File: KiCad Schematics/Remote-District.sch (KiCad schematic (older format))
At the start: 13 parts, among them M1 Fan

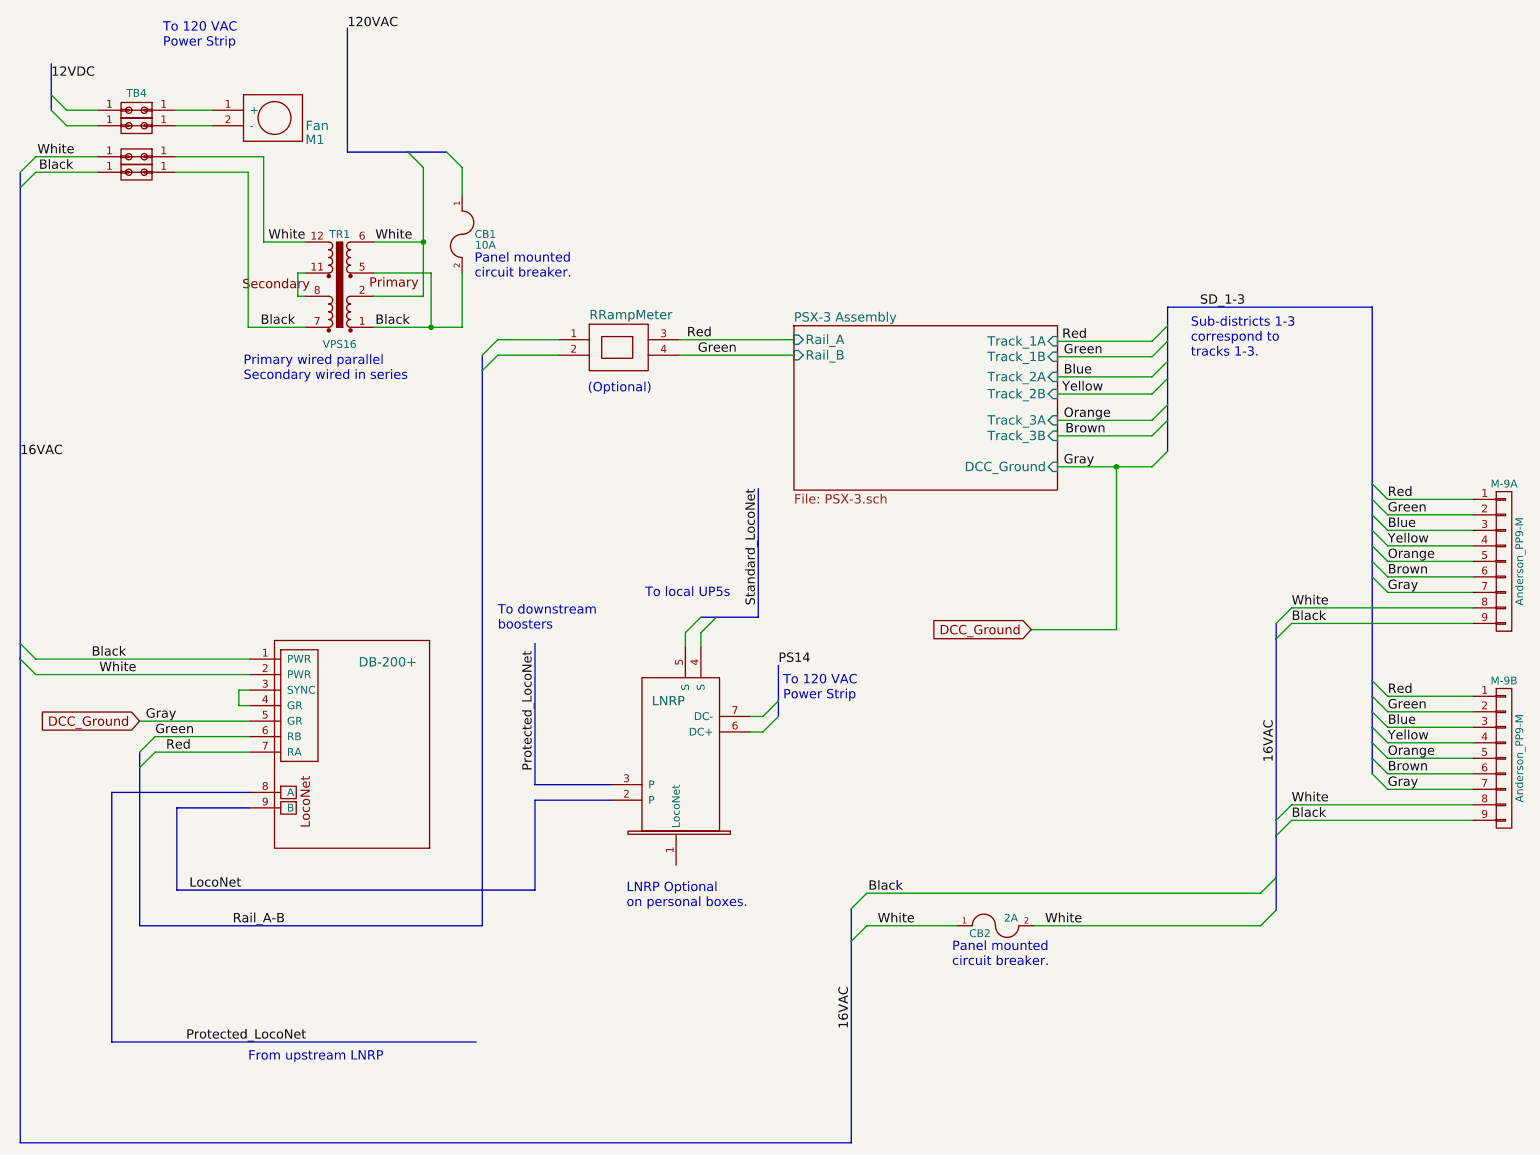
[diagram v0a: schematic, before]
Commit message: Updated schematic for remote boxes
Cleaned up the wiring, removed an unnecessary terminal block and
clarified transformer wiring.
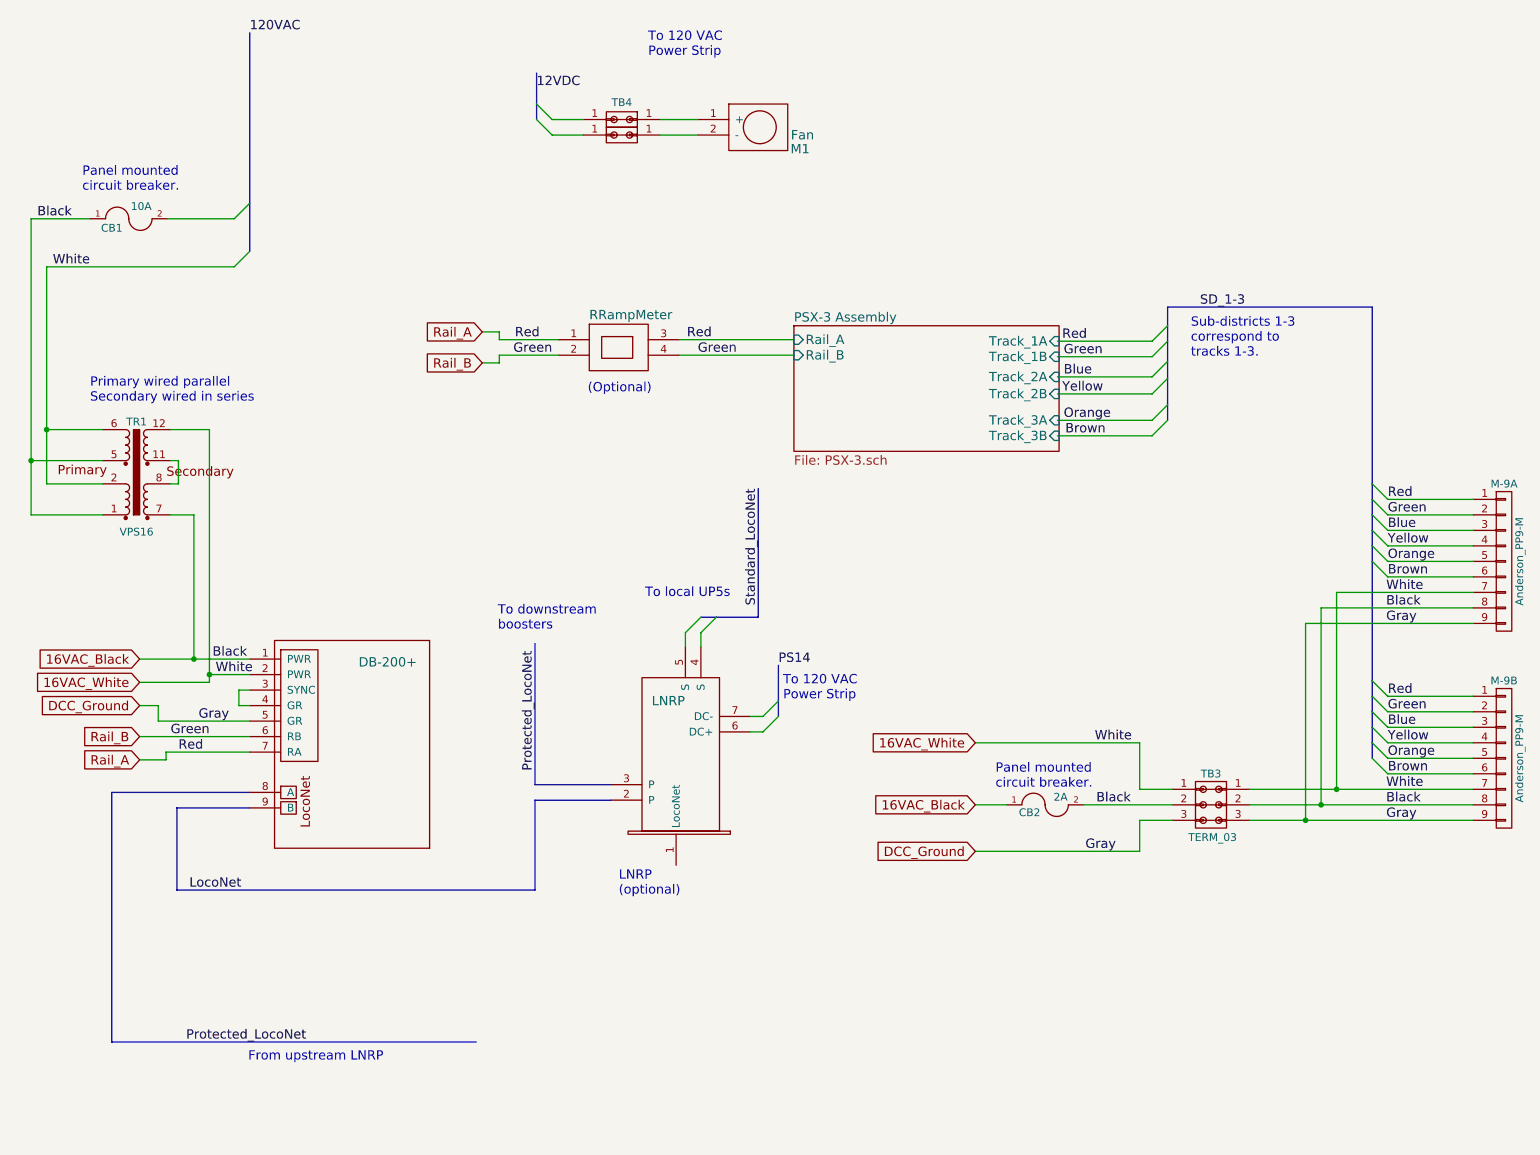
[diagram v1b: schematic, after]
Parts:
- removed TB? (x2): TBLOCK, symbol TBLOCK
- added TB3: TERM_03, symbol TERM_03
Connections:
- net labels added: 16VAC_Black, 16VAC_White, Rail_A, Rail_B
- net labels removed: 16VAC, Rail_A-B
- wire segments 73 -> 87
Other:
- note added: "LNRP\n(optional)"
- note removed: "LNRP Optional\non personal boxes."
- moved on the sheet: 2A, CB1, M1, TR1

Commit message: Updated schematic
Minor cleanup and update of PDF
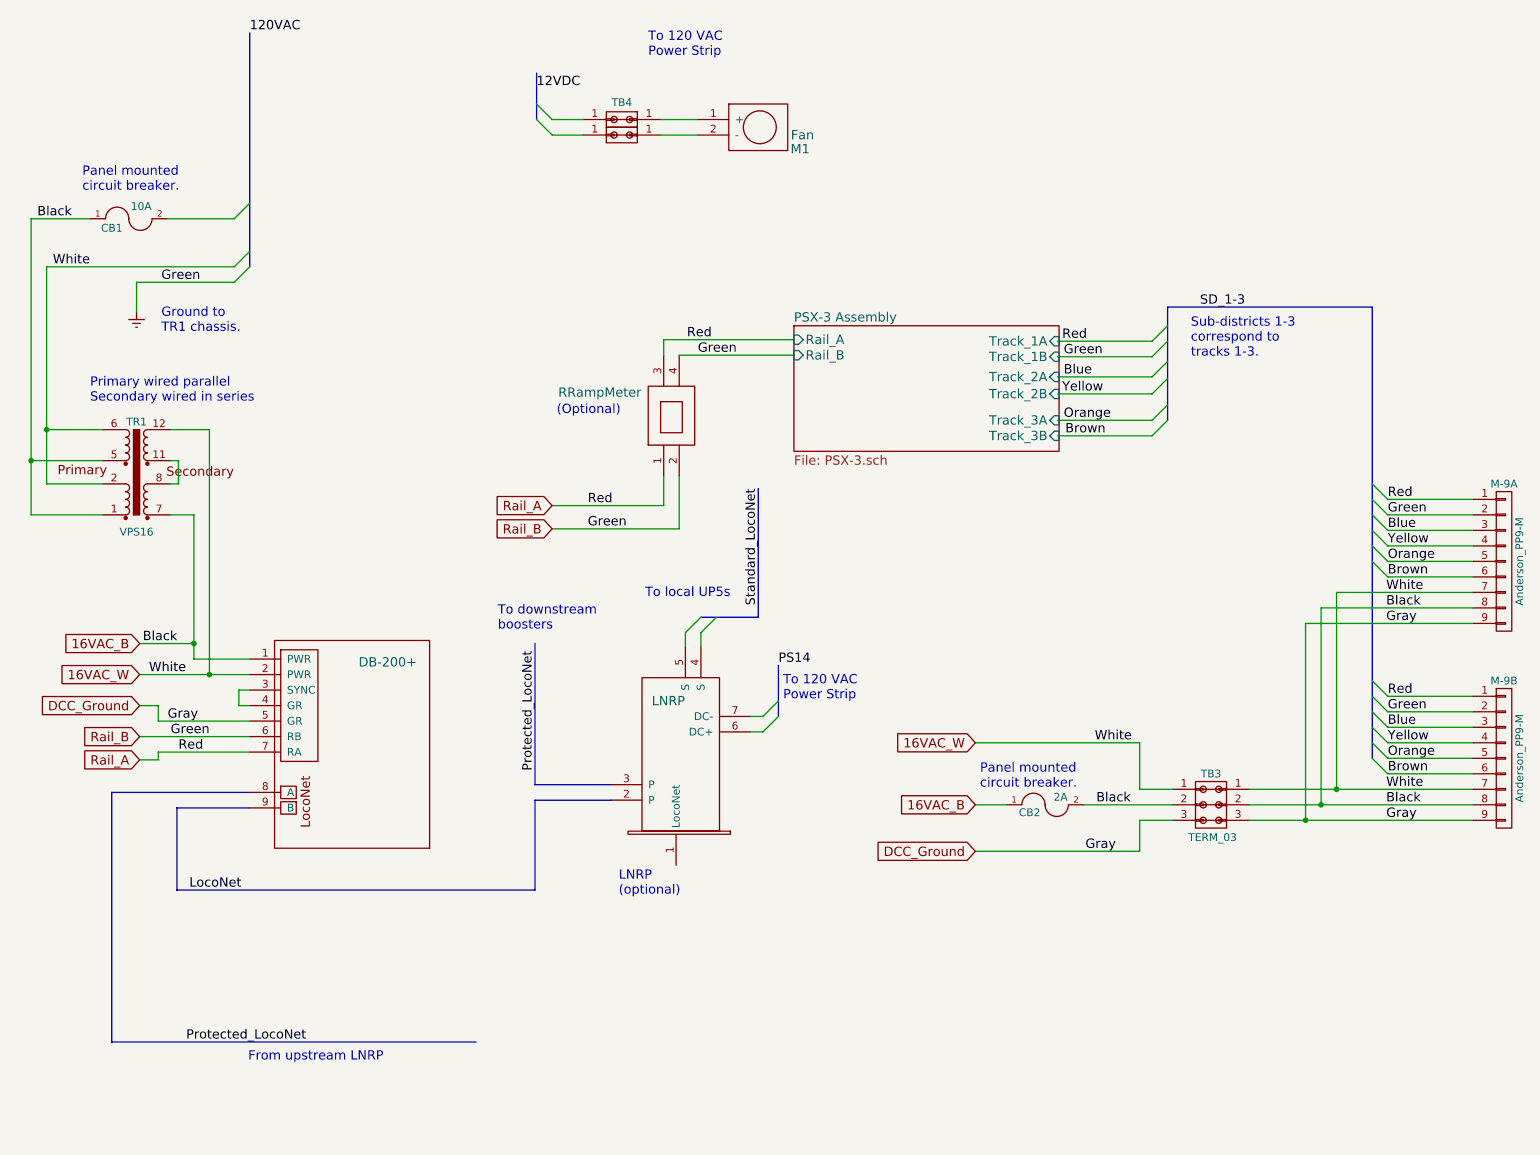
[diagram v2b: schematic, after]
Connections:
- net labels added: 16VAC_B, 16VAC_W, Earth
- net labels removed: 16VAC_Black, 16VAC_White
- wire segments 87 -> 81
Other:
- note added: "Ground to\nTR1 chassis."
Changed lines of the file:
@@
 L RRampmeter M?
 U 1 1 57C1C74E
-P 4220 2530
-F 0 "M?" V 4080 2590 60  0001 C CNN
-F 1 "RRampMeter" V 4160 2530 60  0000 L CNN
-F 2 "" H 4220 2530 60  0000 C CNN
-F 3 "" H 4220 2530 60  0000 C CNN
-	1    4220 2530
-	0    1    1    0
+P 4600 3310
+F 0 "M?" V 4460 3370 60  0001 C CNN
+F 1 "RRampMeter" H 4020 3650 60  0000 L CNN
+F 2 "" H 4600 3310 60  0000 C CNN
+F 3 "" H 4600 3310 60  0000 C CNN
+	1    4600 3310
+	1    0    0    -1
 $EndComp
 Wire Wire Line
@@
 	4180 1310 3980 1310
 Wire Bus Line
-	3880 910  3880 1110
-Wire Bus Line
-	3880 1110 3880 1210
+	3880 910  3880 1210
 Wire Wire Line
 	2030 4890 1960 4890
@@
 	1560 6180 3870 6180
 Wire Wire Line
-	5540 2630 4800 2630
+	4700 2630 5540 2630
 Wire Wire Line
 	5540 2730 4800 2730
@@
 	5340 5160 5440 5060
 Wire Bus Line
-	5440 4730 5440 4960
-Wire Bus Line
-	5440 4960 5440 5060
+	5440 4730 5440 5060
 Text Label 5440 4730 0    60   ~ 0
 PS14
@@
 Sub-districts 1-3\ncorrespond to\ntracks 1-3.
 Wire Bus Line
-	4940 4420 5040 4420
-Wire Bus Line
-	5040 4420 5310 4420
+	4940 4420 5310 4420
 Wire Bus Line
 	5310 4420 5310 3590
@@
 	1    0    0    -1
 $EndComp
-Text Notes 6840 5530 0    60   ~ 0
+Text Notes 6740 5530 0    60   ~ 0
 Panel mounted\ncircuit breaker.
 Wire Wire Line
@@
 Entry Wire Line
 	1930 1850 2030 1750
-Text Notes 4210 2980 0    60   ~ 0
+Text Notes 4010 3120 0    60   ~ 0
 (Optional)
 Text Notes 4410 6220 0    60   ~ 0
@@
 Text Label 1570 5290 0    60   ~ 0
 Red
-Text Label 1700 5090 0    60   ~ 0
+Text Label 1500 5090 0    60   ~ 0
 Gray
-Text Label 1790 4690 0    60   ~ 0
+Text Label 1340 4590 0    60   ~ 0
 Black
-Text Label 1810 4790 0    60   ~ 0
+Text Label 1380 4790 0    60   ~ 0
 White
 Text Label 7480 5230 0    60   ~ 0
@@
 	9370 5430 9270 5330
 Wire Wire Line
-	8480 5730 8840 5730
-Wire Wire Line
-	8840 5730 9920 5730
-Wire Wire Line
-	8480 5630 8940 5630
-Wire Wire Line
-	8940 5630 9920 5630
+	8480 5730 9920 5730
+Wire Wire Line
+	8480 5630 9920 5630
 $Comp
 L CONN_01X09 M-9B
@@
 $EndComp
 Wire Bus Line
-	9270 2420 9270 3560
-Wire Bus Line
-	9270 3560 9270 3660
-Wire Bus Line
-	9270 3660 9270 3760
-Wire Bus Line
-	9270 3760 9270 3860
-Wire Bus Line
-	9270 3860 9270 3960
-Wire Bus Line
-	9270 3960 9270 4060
-Wire Bus Line
-	9270 4060 9270 4830
-Wire Bus Line
-	9270 4830 9270 4930
-Wire Bus Line
-	9270 4930 9270 5030
-Wire Bus Line
-	9270 5030 9270 5130
-Wire Bus Line
-	9270 5130 9270 5230
-Wire Bus Line
-	9270 5230 9270 5330
+	9270 2420 9270 5330
 Text Label 9370 3660 0    60   ~ 0
 Red
@@
 Brown
 Wire Bus Line
-	7950 2420 7950 2540
-Wire Bus Line
-	7950 2540 7950 2640
-Wire Bus Line
-	7950 2640 7950 2770
-Wire Bus Line
-	7950 2770 7950 2880
-Wire Bus Line
-	7950 2880 7950 3050
-Wire Bus Line
-	7950 3050 7950 3150
+	7950 2420 7950 3150
 Wire Bus Line
 	7950 2420 9270 2420
@@
 $EndComp
 Wire Wire Line
-	8480 5530 9040 5530
-Wire Wire Line
-	9040 5530 9920 5530
+	8480 5530 9920 5530
 Wire Wire Line
 	9040 5530 9040 4260
@@
 Wire Wire Line
 	1670 3760 1670 4690
-Connection ~ 1670 4690
 Wire Wire Line
 	1520 3210 1770 3210
 Wire Wire Line
 	1770 3210 1770 4790
-Wire Wire Line
-	1770 4790 1770 4840
 Connection ~ 1770 4790
 Wire Wire Line
 	620  3760 1080 3760
 Wire Wire Line
-	620  1850 620  3410
-Wire Wire Line
-	620  3410 620  3760
+	620  1850 620  3760
 Wire Wire Line
 	1080 3410 620  3410
 Connection ~ 620  3410
 Wire Wire Line
-	720  2160 720  3210
-Wire Wire Line
-	720  3210 720  3560
+	720  2160 720  3560
 Wire Wire Line
 	1080 3210 720  3210
@@
 	1500 1850 1930 1850
 Wire Bus Line
-	2030 650  2030 1750
-Wire Bus Line
-	2030 1750 2030 2060
+	2030 650  2030 2160
 Wire Wire Line
 	720  3560 1080 3560
-Text GLabel 1320 4690 0    60   Input ~ 0
-16VAC_Black
-Text GLabel 1320 4840 0    60   Input ~ 0
-16VAC_White
-Wire Wire Line
-	1320 4690 1670 4690
+Text GLabel 1320 4590 0    60   Input ~ 0
+16VAC_B
+Text GLabel 1320 4790 0    60   Input ~ 0
+16VAC_W
 Wire Wire Line
 	1670 4690 2030 4690
 Wire Wire Line
-	1770 4790 2030 4790
-Wire Wire Line
-	1770 4840 1320 4840
+	1320 4790 2030 4790
 Text GLabel 6710 5630 0    60   Input ~ 0
-16VAC_Black
+16VAC_B
 Text GLabel 6710 5230 0    60   Input ~ 0
-16VAC_White
+16VAC_W
 Wire Wire Line
 	6910 5630 6710 5630
@@
 	2030 5190 1320 5190
 Wire Wire Line
-	2030 5290 1490 5290
-Wire Wire Line
-	1490 5290 1490 5340
-Wire Wire Line
-	1490 5340 1320 5340
-Text GLabel 3530 2580 0    60   Input ~ 0
+	2030 5290 1440 5290
+Wire Wire Line
+	1440 5290 1440 5340
+Wire Wire Line
+	1440 5340 1320 5340
+Text GLabel 3980 3700 0    60   Input ~ 0
 Rail_A
-Text GLabel 3530 2780 0    60   Input ~ 0
+Text GLabel 3980 3850 0    60   Input ~ 0
 Rail_B
-Wire Wire Line
-	4020 2630 3640 2630
-Wire Wire Line
-	3640 2630 3640 2580
-Wire Wire Line
-	3640 2580 3530 2580
-Wire Wire Line
-	4020 2730 3640 2730
-Wire Wire Line
-	3640 2730 3640 2780
-Wire Wire Line
-	3640 2780 3530 2780
-Text Label 3740 2630 0    60   ~ 0
+Text Label 4210 3700 0    60   ~ 0
 Red
-Text Label 3730 2730 0    60   ~ 0
+Text Label 4210 3850 0    60   ~ 0
 Green
 Wire Wire Line
@@
 Wire Wire Line
 	1440 5090 2030 5090
+Wire Wire Line
+	1320 4590 1670 4590
+Connection ~ 1670 4590
+Wire Wire Line
+	4700 2630 4700 2730
+Wire Wire Line
+	3980 3700 4700 3700
+Wire Wire Line
+	4700 3700 4700 3510
+Wire Wire Line
+	3980 3850 4800 3850
+Wire Wire Line
+	4800 3850 4800 3510
+Entry Wire Line
+	1930 2260 2030 2160
+Wire Wire Line
+	1930 2260 1300 2260
+Wire Wire Line
+	1300 2260 1300 2450
+$Comp
+L Earth #PWR?
+U 1 1 57FD578E
+P 1300 2450
+F 0 "#PWR?" H 1300 2200 50  0001 C CNN
+F 1 "Earth" H 1300 2300 50  0001 C CNN
+F 2 "" H 1300 2450 50  0000 C CNN
+F 3 "" H 1300 2450 50  0000 C CNN
+	1    1300 2450
+	1    0    0    -1
+$EndComp
+Text Label 1460 2260 0    60   ~ 0
+Green
+Text Notes 1460 2590 0    60   ~ 0
+Ground to\nTR1 chassis.
 $EndSCHEMATC

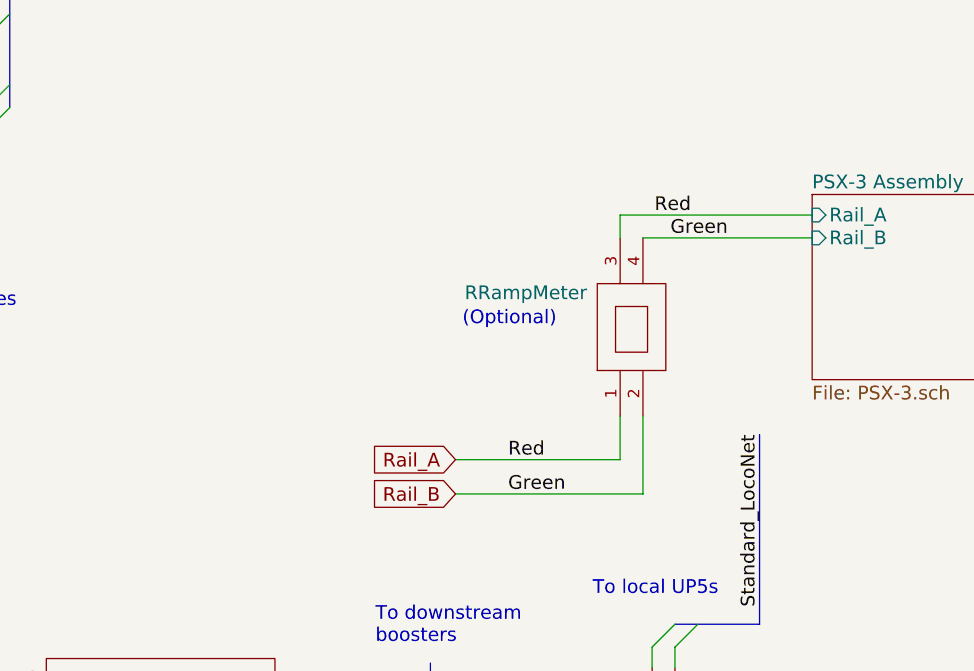
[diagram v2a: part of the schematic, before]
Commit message: Simplified schematic
Minor change to remote box wiring to simplify visual.
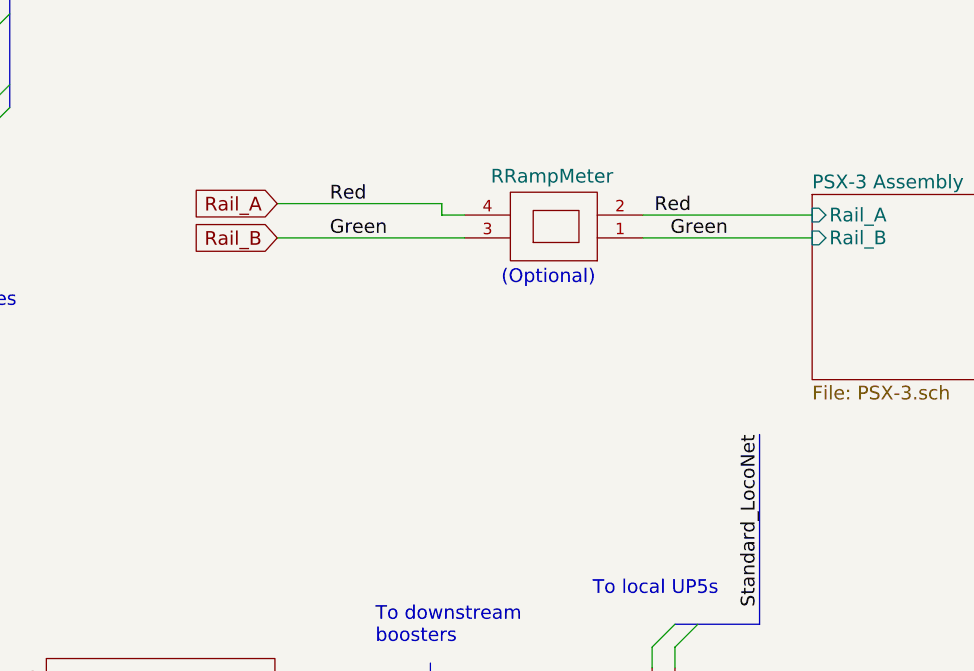
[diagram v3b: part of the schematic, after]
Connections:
- wire segments 81 -> 80
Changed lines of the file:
@@
 L RRampmeter M?
 U 1 1 57C1C74E
-P 4600 3310
-F 0 "M?" V 4460 3370 60  0001 C CNN
-F 1 "RRampMeter" H 4020 3650 60  0000 L CNN
-F 2 "" H 4600 3310 60  0000 C CNN
-F 3 "" H 4600 3310 60  0000 C CNN
-	1    4600 3310
-	1    0    0    -1
+P 4600 2830
+F 0 "M?" V 4460 2890 60  0001 C CNN
+F 1 "RRampMeter" V 4970 2760 60  0000 L CNN
+F 2 "" H 4600 2830 60  0000 C CNN
+F 3 "" H 4600 2830 60  0000 C CNN
+	1    4600 2830
+	0    -1   -1   0
 $EndComp
 Wire Wire Line
@@
 	1560 6180 3870 6180
 Wire Wire Line
-	4700 2630 5540 2630
+	4800 2630 5540 2630
 Wire Wire Line
 	5540 2730 4800 2730
@@
 Entry Wire Line
 	1930 1850 2030 1750
-Text Notes 4010 3120 0    60   ~ 0
+Text Notes 4180 2940 0    60   ~ 0
 (Optional)
 Text Notes 4410 6220 0    60   ~ 0
@@
 Wire Wire Line
 	1440 5340 1320 5340
-Text GLabel 3980 3700 0    60   Input ~ 0
+Text GLabel 3200 2580 0    60   Input ~ 0
 Rail_A
-Text GLabel 3980 3850 0    60   Input ~ 0
+Text GLabel 3200 2730 0    60   Input ~ 0
 Rail_B
-Text Label 4210 3700 0    60   ~ 0
+Text Label 3430 2580 0    60   ~ 0
 Red
-Text Label 4210 3850 0    60   ~ 0
+Text Label 3430 2730 0    60   ~ 0
 Green
 Wire Wire Line
@@
 Connection ~ 1670 4590
 Wire Wire Line
-	4700 2630 4700 2730
-Wire Wire Line
-	3980 3700 4700 3700
-Wire Wire Line
-	4700 3700 4700 3510
-Wire Wire Line
-	3980 3850 4800 3850
-Wire Wire Line
-	4800 3850 4800 3510
+	3200 2580 3920 2580
+Wire Wire Line
+	3200 2730 4020 2730
 Entry Wire Line
 	1930 2260 2030 2160
@@
 Text Notes 1460 2590 0    60   ~ 0
 Ground to\nTR1 chassis.
+Wire Wire Line
+	4020 2630 3920 2630
+Wire Wire Line
+	3920 2630 3920 2580
 $EndSCHEMATC
